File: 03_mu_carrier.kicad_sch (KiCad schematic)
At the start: 42 parts, among them J10 M.2 M-key NVMe (x1), J8 Mu SIO UART debug (verify IO 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, J9 RTC backup coin-cell header, SW2 Mu Power, SW3 Mu Reset, U6 SY8253ADC VSYS -> SYS_5V, U7 SY8253ADC VSYS -> SYS_3V3, U8 TPS7A0210 (VL822 1.0V), U9 VL822-Q7, Y3 25MHz (VL822)

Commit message: Publish the current Ducktop2 design
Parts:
- removed C40: 10u VIN, Capacitor_SMD:C_1206_3216Metric, symbol Device:C
- removed C41: 100n BOOT, Capacitor_SMD:C_0603_1608Metric, symbol Device:C
- removed C52: 1u IN, Capacitor_SMD:C_0805_2012Metric, symbol Device:C
- removed C53: 1u OUT, Capacitor_SMD:C_0805_2012Metric, symbol Device:C
- removed C54, C55, C56, C57, C58, C59: 100n hub bypass, Capacitor_SMD:C_0603_1608Metric, symbol Device:C
- removed C60, C61, C62, C63: 100n hub 1V0 bypass, Capacitor_SMD:C_0603_1608Metric, symbol Device:C
- removed C64, C65: 18p, Capacitor_SMD:C_0603_1608Metric, symbol Device:C
- removed U6: SY8253ADC VSYS -> SYS_5V, Package_TO_SOT_SMD:TSOT-23-6, symbol ducktop2:SY8253ADC
- removed U8: TPS7A0210 (VL822 1.0V), ducktop2:X2SON-4_1.0x1.0mm_P0.65mm, symbol ducktop2:TPS7A0210
- removed U9: VL822-Q7, ducktop2:QFN-76-1EP_9x9mm_P0.4mm_EP6.3x6.3mm, symbol ducktop2:VL822-Q7
- removed Y3: 25MHz (VL822), Crystal:Crystal_SMD_3225-4Pin_3.2x2.5mm, symbol Device:Crystal_GND24
- added C44, C45, C792: 22u 16V X7R TPS56637 OUT, Capacitor_SMD:C_1206_3216Metric, symbol Device:C
- added C586, C587, C66, C67: 100n 10V X7R Mu USB3 TX AC, Capacitor_SMD:C_0402_1005Metric, symbol Device:C
- added C590, C591: 220n 10V X7R Wi-Fi TX AC, Capacitor_SMD:C_0402_1005Metric, symbol Device:C
- added C592, C593, C594, C595, C596, C597, C68, C69: 220n 10V X7R NVMe TX AC, Capacitor_SMD:C_0402_1005Metric, symbol Device:C
- added C750: 68u 50V hybrid input bulk, Capacitor_SMD:CP_Elec_8x10, symbol Device:C_Polarized
- added C751, C752: 10u 50V X7R input, Capacitor_SMD:C_1206_3216Metric, symbol Device:C
- added C753: 1u 50V X5R input, Capacitor_SMD:C_0603_1608Metric, symbol Device:C
- added C754, C755: 100n 50V X7R input HF, Capacitor_SMD:C_0402_1005Metric, symbol Device:C
- added C756, C757: 100n 50V X7R output HF, Capacitor_SMD:C_0402_1005Metric, symbol Device:C
- added C758: 1u 50V X5R output, Capacitor_SMD:C_0603_1608Metric, symbol Device:C
- added C759, C760, C761: 10u 50V X7R output, Capacitor_SMD:C_1206_3216Metric, symbol Device:C
- added C762: 100u 35V hybrid output bulk, Capacitor_SMD:CP_Elec_6.3x5.8, symbol Device:C_Polarized
- added C763: 1u 50V post-sense load-side bypass, Capacitor_SMD:C_0603_1608Metric, symbol Device:C
- added C764: 22u 16V X7R VCC mandatory; effective >4.7u, Capacitor_SMD:C_1206_3216Metric, symbol Device:C
- added C765, C766: 100n 50V X8L bootstrap, Capacitor_SMD:C_0603_1608Metric, symbol Device:C
- added C767: 10n DITH/SYNC spreading, Capacitor_SMD:C_0603_1608Metric, symbol Device:C
- added C768, C769: DNP 2.2n 250V X7R switch-node snubber, Capacitor_SMD:C_0805_2012Metric, symbol Device:C
- added C770: 100n differential current-sense filter, Capacitor_SMD:C_0603_1608Metric, symbol Device:C
- added C771: 4.7n COMP, Capacitor_SMD:C_0603_1608Metric, symbol Device:C
- added C772: 100p C0G COMP HF, Capacitor_SMD:C_0603_1608Metric, symbol Device:C
- added C773: 100n UVLO noise filter, Capacitor_SMD:C_0603_1608Metric, symbol Device:C
- added C774: 10n PG deglitch, Capacitor_SMD:C_0603_1608Metric, symbol Device:C
- added C775: 10n CC deglitch, Capacitor_SMD:C_0603_1608Metric, symbol Device:C
- added C790: 10u 50V X7R TPS56637 VIN, Capacitor_SMD:C_1206_3216Metric, symbol Device:C
- added C791: 100n 50V X7R TPS56637 VIN HF, Capacitor_SMD:C_0603_1608Metric, symbol Device:C
- added C793: 100n qualified host-active gate local, Capacitor_SMD:C_0603_1608Metric, symbol Device:C
- added C794: 1u internal host VBUS switch input, Capacitor_SMD:C_0805_2012Metric, symbol Device:C
- added C830: 10u internal host VBUS output, Capacitor_SMD:C_1206_3216Metric, symbol Device:C
- added C831: 100n internal VBUS supervisor local, Capacitor_SMD:C_0603_1608Metric, symbol Device:C
- added C832: 1u PCIe endpoint switch input, Capacitor_SMD:C_0805_2012Metric, symbol Device:C
- added C833: 4.7n PCIe endpoint controlled slew, Capacitor_SMD:C_0402_1005Metric, symbol Device:C
- added C834: 47u 6.3V PCIe endpoint rail bulk, Capacitor_SMD:C_1206_3216Metric, symbol Device:C
- added C835: 100n PCIe endpoint rail HF, Capacitor_SMD:C_0603_1608Metric, symbol Device:C
- added C836: 10u 6.3V NVMe socket local bulk, Capacitor_SMD:C_1206_3216Metric, symbol Device:C
- added C837: 100n NVMe socket local HF, Capacitor_SMD:C_0603_1608Metric, symbol Device:C
- added H1: Wurth 9774055243R Mu M2 standoff 5.5mm A, ducktop2:Wurth_9774055243R_M2_H5.5, symbol Mechanical:MountingHole_Pad
- added H10, H11, H12, H13, H14, H15, H16, H17: M2.5 isolated mainboard mounting hole, MountingHole:MountingHole_2.7mm_M2.5, symbol Mechanical:MountingHole
- added H2: Wurth 9774055243R Mu M2 standoff 5.5mm B, ducktop2:Wurth_9774055243R_M2_H5.5, symbol Mechanical:MountingHole_Pad
- added H3: M.2 M-key 2280 M2 grounded standoff 2.5mm, ducktop2:SMT_Standoff_M2_H2.5_C4_Tail2.7x1.5, symbol Mechanical:MountingHole_Pad
- added L750: 4.7uH 10.1A Isat / 6.9A Irms, Inductor_SMD:L_Coilcraft_XAL7030-472, symbol Device:L
- added Q750: BSS138 fail-off EN/UVLO clamp, Package_TO_SOT_SMD:SOT-23, symbol Q_NMOS_SOT23_GSD:Q_NMOS_SOT23_GSD
- added Q751: BSS138 active-high enable release, Package_TO_SOT_SMD:SOT-23, symbol Q_NMOS_SOT23_GSD:Q_NMOS_SOT23_GSD
- added R40: 76.8k 0.1% TPS56637 FB high, Resistor_SMD:R_0603_1608Metric, symbol Device:R
- added R41: 10k 0.1% TPS56637 FB low, Resistor_SMD:R_0603_1608Metric, symbol Device:R
- added R42, R770: 169k 1% TPS56637 EN high, Resistor_SMD:R_0603_1608Metric, symbol Device:R
- added R50: 1k NVMe CLKREQ# low: request REFCLK, Resistor_SMD:R_0603_1608Metric, symbol Device:R
- added R750: 10R ISP Kelvin filter, Resistor_SMD:R_0603_1608Metric, symbol Device:R
- added R751: 10R ISN Kelvin filter, Resistor_SMD:R_0603_1608Metric, symbol Device:R
- added R752: 49.9R FB isolation, Resistor_SMD:R_0603_1608Metric, symbol Device:R
- added R753: 102k 0.1% 12V FB high, Resistor_SMD:R_0603_1608Metric, symbol Device:R
- added R754: 11.3k 0.1% 12V FB low, Resistor_SMD:R_0603_1608Metric, symbol Device:R
- added R755: 15k COMP series, Resistor_SMD:R_0603_1608Metric, symbol Device:R
- added R756: 49.9k 1% FSW = 400kHz, Resistor_SMD:R_0603_1608Metric, symbol Device:R
- added R757: 0R MODE forced-PWM, Resistor_SMD:R_0603_1608Metric, symbol Device:R
- added R758: 0R EXTVCC selects internal LDO, Resistor_SMD:R_0603_1608Metric, symbol Device:R
- added R759: 150k 1% UVLO high; 9.0V rising, Resistor_SMD:R_0603_1608Metric, symbol Device:R
- added R760: 23.7k 1% UVLO low, Resistor_SMD:R_0603_1608Metric, symbol Device:R
- added R761: 100k fail-off gate divider low, Resistor_SMD:R_0603_1608Metric, symbol Device:R
- added R762: 100k PG pull-up, Resistor_SMD:R_0603_1608Metric, symbol Device:R
- added R763: 100k CC pull-up, Resistor_SMD:R_0603_1608Metric, symbol Device:R
- added R764, R765: DNP 2.2R 0.25W switch-node snubber, Resistor_SMD:R_1206_3216Metric, symbol Device:R
- added R766: 100k fail-off gate divider high, Resistor_SMD:R_0603_1608Metric, symbol Device:R
- added R767: 100k MU_12V_ENABLE reset pulldown, Resistor_SMD:R_0603_1608Metric, symbol Device:R
- added R768: 10k LattePanda PSON required pull-up, Resistor_SMD:R_0603_1608Metric, symbol Device:R
- added R769: 100k MU_HOST_ACTIVE fail-low, Resistor_SMD:R_0603_1608Metric, symbol Device:R
- added R771: 36.1k 1% TPS56637 EN low, Resistor_SMD:R_0603_1608Metric, symbol Device:R
- added R772: 100k SYS_3V3 PG pull-up, Resistor_SMD:R_0603_1608Metric, symbol Device:R
- added R773: 43.2k 1% internal host VBUS 0.61A ILIM, Resistor_SMD:R_0603_1608Metric, symbol Device:R
- added R774: 10k internal host VBUS fault pull-up, Resistor_SMD:R_0603_1608Metric, symbol Device:R
- added R775: 10k internal host VBUS valid pull-up, Resistor_SMD:R_0603_1608Metric, symbol Device:R
- added R776: 100k PCIe endpoint rail fail-low, Resistor_SMD:R_0603_1608Metric, symbol Device:R
- added RS750: 15mOhm 1% 1W; 3.33A output current limit, Resistor_SMD:R_1206_3216Metric, symbol Device:R
- added SW2: Mu Power, Button_Switch_SMD:SW_SPST_B3S-1000, symbol Switch:SW_Push
- added TP12: MU_12V_PG test, TestPoint:TestPoint_Pad_D1.0mm, symbol Connector:TestPoint
- added TP13: Internal USB VBUS test, TestPoint:TestPoint_Pad_D1.0mm, symbol Connector:TestPoint
- added TP14: Internal USB VBUS valid test, TestPoint:TestPoint_Pad_D1.0mm, symbol Connector:TestPoint
- added TP15: Internal USB VBUS fault test, TestPoint:TestPoint_Pad_D1.0mm, symbol Connector:TestPoint
- added TP5: SYS_5V test, TestPoint:TestPoint_Pad_D1.0mm, symbol Connector:TestPoint
- added TP6: SYS_3V3 test, TestPoint:TestPoint_Pad_D1.0mm, symbol Connector:TestPoint
- added TP8: MU_12V test, TestPoint:TestPoint_Pad_D1.0mm, symbol Connector:TestPoint
- added U6: TPS56637RPAR VSYS -> SYS_5V (5.10V, 6A class), ducktop2:Texas_RPA0010A_VQFN-HR-10_3x3mm, symbol TPS56637:TPS56637
- added U7: TPS56637RPAR VSYS -> SYS_3V3 (3.32V, 6A class), ducktop2:Texas_RPA0010A_VQFN-HR-10_3x3mm, symbol TPS56637:TPS56637
- added U750: TPS552892RYQR 12V buck-boost, ducktop2:Texas_RYQ0021A_VQFN-HR-21_3x5mm, symbol TPS552892:TPS552892
- added U769: SN74LVC1G08DBVR qualified host-active AND, Package_TO_SOT_SMD:SOT-23-5, symbol 74xGxx:74LVC1G08
- added U770: TPS2553DDBVR internal host VBUS 0.61A, Package_TO_SOT_SMD:SOT-23-6, symbol TPS2553D:TPS2553D
- added U771: TLV803EA43RDBZR 4.38V physical internal VBUS supe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, Package_TO_SOT_SMD:SOT-23-3, symbol TLV803EA43RDBZR:TLV803EA43RDBZR
- added U772: TPS22975NDSGR switched PCIe endpoint 3V3, Package_SON:Texas_DSG0008A_WSON-8-1EP_2x2mm_P0.5mm_EP0.9x1.6mm, symbol TPS22975N:TPS22975N
- A1: value LattePanda Mu -> TE 2309411-1 LattePanda Mu host socket/interface; BIOSProfile (none) -> DFLT S70NC1R200-16G-B.bin; SHA256 6edcfe021d84baf2b6ea3e4f4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; MPN (none) -> 2309411-1; Manufacturer (none) -> TE Connectivity; ModuleAssemblyItem (none) -> A2 DFRobot DFR1149; SocketHeight (none) -> 8.0mm standard orientation
- A2: renamed from SW2; value Mu Power -> DFR1149 LattePanda Mu N305 16GB/64GB removable module; footprint Button_Switch_SMD:SW_SPST_B3S-1000 -> (none); symbol Switch:SW_Push -> Mechanical:MountingHole; AssemblyType (none) -> Customer-fitted removable compute module; BIOSProfile (none) -> DFLT S70NC1R200-16G-B.bin; build 2026-06-03; SHA256 6edcfe0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; MPN (none) -> DFR1149; Manufacturer (none) -> DFRobot; RequiredSocket (none) -> A1 TE Connectivity 2309411-1
- C40: renamed from R40; value 732k 1% -> 10u 50V X7R TPS56637 VIN; footprint Resistor_SMD:R_0603_1608Metric -> Capacitor_SMD:C_1206_3216Metric; symbol Device:R -> Device:C; MPN (none) -> CGA5L1X7R1H106K160AC; Manufacturer (none) -> TDK
- C41: renamed from R41; value 100k 1% -> 10u 50V X7R TPS56637 VIN; footprint Resistor_SMD:R_0603_1608Metric -> Capacitor_SMD:C_1206_3216Metric; symbol Device:R -> Device:C; MPN (none) -> CGA5L1X7R1H106K160AC; Manufacturer (none) -> TDK
- C42: value 22u OUT -> 100n 50V X7R TPS56637 VIN HF; footprint Capacitor_SMD:C_1206_3216Metric -> Capacitor_SMD:C_0603_1608Metric
- C43: renamed from U7; value SY8253ADC VSYS -> SYS_3V3 -> 100n 16V X7R TPS56637 BOOT; footprint Package_TO_SOT_SMD:TSOT-23-6 -> Capacitor_SMD:C_0603_1608Metric; symbol ducktop2:SY8253ADC -> Device:C
- C46: value 10u VIN -> 10u 50V X7R TPS56637 VIN; MPN (none) -> CGA5L1X7R1H106K160AC; Manufacturer (none) -> TDK
- C47: value 100n BOOT -> 100n 16V X7R TPS56637 BOOT
- C48: value 22u OUT -> 22u 16V X7R TPS56637 OUT; MPN (none) -> GRM31CZ71C226ME15L; Manufacturer (none) -> Murata
- J10: value M.2 M-key NVMe (x1) -> Amphenol MDT420M01001 M-key NVMe socket (PCIe x4); footprint Connector_PCBEdge:M.2_2280-xx-M -> ducktop2:Amphenol_MDT420M01001_H4.2; MPN (none) -> MDT420M01001; Manufacturer (none) -> Amphenol
- J8: value Mu SIO UART debug (verify IO voltage) -> DNP Mu SIO UART debug (IO voltage unverified); now not fitted; now left out of the parts list
- J9: footprint Connector_PinHeader_2.54mm:PinHeader_1x02_P2.54mm_Vertical -> Connector_JST:JST_GH_SM02B-GHS-TB_1x02-1MP_P1.25mm_Horizontal; Contacts (none) -> SSHL-002T-P0.2; MPN (none) -> SM02B-GHS-TB; Manufacturer (none) -> JST; MatingHousing (none) -> GHR-02V-S
- L4: value 2.2uH >=4.3A -> XAL7070-332MEC 3.3uH 19.4A Isat30%; footprint Inductor_SMD:L_1210_3225Metric -> Inductor_SMD:L_Coilcraft_XAL7070-XXX; MPN (none) -> XAL7070-332MEC; Manufacturer (none) -> Coilcraft
- L5: value 2.2uH >=4.3A -> XAL7070-222MEC 2.2uH 19.6A Isat30%; footprint Inductor_SMD:L_1210_3225Metric -> Inductor_SMD:L_Coilcraft_XAL7070-XXX; MPN (none) -> XAL7070-222MEC; Manufacturer (none) -> Coilcraft
- R43: value 450k 1% -> 45.3k 1% TPS56637 FB high
- R44: value 100k 1% -> 10k 1% TPS56637 FB low
- R45: value 12.1k (verify VL822 REXT) -> 36.1k 1% TPS56637 EN low
- R46: value 100k -> 100k SYS_5V PG pull-up
- SW3: MPN (none) -> B3S-1000; Manufacturer (none) -> Omron
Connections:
- net BUCK33_BOOT: now also U7.7 (BOOT); no longer C43.1 (BOOST)
- net BUCK33_FB: now also U7.2 (FB); no longer C43.3 (FB)
- net BUCK33_SW: now also U7.6 (SW); no longer C43.6 (SW)
- net BUCK5_BOOT: now also C43.1, U6.7 (BOOT)
- net BUCK5_FB: now also R40.2, R41.1, U6.2 (FB); no longer C40.2, C41.1
- net BUCK5_SW: now also C43.2, U6.6 (SW)
- net GND: now also C40.2, C44.2, C45.2, C750.2, C751.2, C752.2, C753.2, C754.2, C755.2, C756.2, C757.2, C758.2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; no longer A2.2, C43.2 (GND)
- net MU_PWRBTN_N: now also SW2.1; no longer A2.1
- net PCIE_M_REFCLK_SRC_N: now also A1.99 (REFCLK2-); no longer A1.87 (REFCLK0-)
- net PCIE_M_REFCLK_SRC_P: now also A1.97 (REFCLK2+); no longer A1.85 (REFCLK0+)
- net SYS_3V3: now also C792.1, C832.1, TP6.1, U772.1 (VIN), U772.2 (VIN), U772.4 (VBIAS); no longer J10.12 (3.3V), J10.14 (3.3V), J10.16 (3.3V), J10.18 (3.3V), J10.2 (3.3V), J10.4 (3.3V), J10.70 (3.3V), J10.72 (3.3V), J10.74 (3.3V), R46.1
- net SYS_5V: now also C44.1, C45.1, C794.1, R40.1, TP5.1, U770.1 (IN); no longer C40.1, C42.1
- net VSYS: now also C40.1, C41.1, C42.1, C750.1, C751.1, C752.1, C753.1, C754.1, C755.1, C790.1, C791.1, R42.1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; no longer A1.250 (VIN), A1.251 (VIN), A1.252 (VIN), A1.253 (VIN), A1.254 (VIN), A1.255 (VIN), A1.256 (VIN), A1.257 (VIN), A1.258 (VIN), A1.259 (VIN), A1.260 (VIN), C43.4 (EN)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
- net WIFI_PCIE_RX_N: now also A1.36 (HSIO3_RX-); no longer A1.24 (HSIO1_RX-)
- net WIFI_PCIE_RX_P: now also A1.34 (HSIO3_RX+); no longer A1.22 (HSIO1_RX+)
- net WIFI_PCIE_TX_N: now also C591.2; no longer A1.21 (HSIO1_TX-)
- net WIFI_PCIE_TX_P: now also C590.2; no longer A1.19 (HSIO1_TX+)
- net WIFI_REFCLK_N: now also A1.90 (REFCLK3-); no longer A1.93 (REFCLK1-)
- net WIFI_REFCLK_P: now also A1.88 (REFCLK3+); no longer A1.91 (REFCLK1+)
- net GBE_CLKREQ_N: now reaches A1.102 (~{CLKREQ4})
- net MU_USB_OC_N: now reaches A1.129 (~{USB_OC})
- net WIFI_PCIE_TX_RAW_P: now reaches A1.31 (HSIO3_TX+)
- net WIFI_PCIE_TX_RAW_P: now also C590.1
- net WIFI_PCIE_TX_RAW_N: now reaches A1.33 (HSIO3_TX-)
- net WIFI_PCIE_TX_RAW_N: now also C591.1
- net PCIE_M_L0_TX_RAW_P: now reaches A1.37 (HSIO8_TX+)
- net PCIE_M_L0_TX_RAW_P: now also C68.1
- net PCIE_M_L0_TX_RAW_N: now reaches A1.39 (HSIO8_TX-)
- net PCIE_M_L0_TX_RAW_N: now also C69.1
- net PCIE_M_L0_RX_P: now reaches A1.40 (HSIO8_RX+)
- net PCIE_M_L0_RX_P: now also J10.43 (PERp0/SATA-B-)
- net PCIE_M_L0_RX_N: now reaches A1.42 (HSIO8_RX-)
- net PCIE_M_L0_RX_N: now also J10.41 (PERn0/SATA-B+)
- net PCIE_M_L1_TX_RAW_P: now reaches A1.43 (HSIO9_TX+)
- net PCIE_M_L1_TX_RAW_P: now also C592.1
- net PCIE_M_L1_TX_RAW_N: now reaches A1.45 (HSIO9_TX-)
- net PCIE_M_L1_TX_RAW_N: now also C593.1
- net PCIE_M_L1_RX_P: now reaches A1.46 (HSIO9_RX+)
- net PCIE_M_L1_RX_P: now also J10.31 (PERp1)
- net PCIE_M_L1_RX_N: now reaches A1.48 (HSIO9_RX-)
- net PCIE_M_L1_RX_N: now also J10.29 (PERn1)
- net PCIE_M_L2_TX_RAW_P: now reaches A1.49 (HSIO10_TX+)
- net PCIE_M_L2_TX_RAW_P: now also C594.1
- net MU_S0_HIGH: now reaches A1.5 (PSON)
- net MU_S0_HIGH: now also R768.2, U769.1
- net PCIE_M_L2_TX_RAW_N: now reaches A1.51 (HSIO10_TX-)
- net PCIE_M_L2_TX_RAW_N: now also C595.1
- net PCIE_M_L2_RX_P: now reaches A1.52 (HSIO10_RX+)
- net PCIE_M_L2_RX_P: now also J10.19 (PERp2)
- net PCIE_M_L2_RX_N: now reaches A1.54 (HSIO10_RX-)
- net PCIE_M_L2_RX_N: now also J10.17 (PERn2)
- net PCIE_M_L3_TX_RAW_P: now reaches A1.55 (HSIO11_TX+)
- net PCIE_M_L3_TX_RAW_P: now also C596.1
- net PCIE_M_L3_TX_RAW_N: now reaches A1.57 (HSIO11_TX-)
- net PCIE_M_L3_TX_RAW_N: now also C597.1
- net PCIE_M_L3_RX_P: now reaches A1.58 (HSIO11_RX+)
- net PCIE_M_L3_RX_P: now also J10.7 (PERp3)
- net PCIE_M_L3_RX_N: now reaches A1.60 (HSIO11_RX-)
- net PCIE_M_L3_RX_N: now also J10.5 (PERn3)
- net GBE_HOST_TX_P: now reaches A1.61 (HSIO6_TX+)
- net GBE_HOST_TX_N: now reaches A1.63 (HSIO6_TX-)
- net GBE_HOST_RX_P: now reaches A1.64 (HSIO6_RX+)
- net GBE_HOST_RX_N: now reaches A1.66 (HSIO6_RX-)
- net GBE_REFCLK_P: now reaches A1.94 (REFCLK4+)
- net GBE_REFCLK_N: now reaches A1.96 (REFCLK4-)
- net PCIE_M_L3_TX_N: now reaches J10.11 (PETn3)
- net PCIE_M_L3_TX_N: now also C597.2
- net PCIE_M_L3_TX_P: now reaches J10.13 (PETp3)
- net PCIE_M_L3_TX_P: now also C596.2
- net PCIE_M_L2_TX_N: now reaches J10.23 (PETn2)
- net PCIE_M_L2_TX_N: now also C595.2
- net PCIE_M_L2_TX_P: now reaches J10.25 (PETp2)
- net PCIE_M_L2_TX_P: now also C594.2
- net PCIE_M_L1_TX_N: now reaches J10.35 (PETn1)
- net PCIE_M_L1_TX_N: now also C593.2
- net PCIE_M_L1_TX_P: now reaches J10.37 (PETp1)
- net PCIE_M_L1_TX_P: now also C592.2
- net PCIE_M_CLKREQ_N: now reaches J10.52 (~{CLKREQ})
- net PCIE_M_CLKREQ_N: now also R50.1
- net DDIB_DDC_SCL: no longer names the net of A1.171 (DDIB_DDC_SCL)
- net DDIB_DDC_SDA: no longer names the net of A1.169 (DDIB_DDC_SDA)
- net DDIB_HPD: no longer names the net of A1.183 (DDIB_HPD)
- net DDIB_TX0_N: no longer names the net of A1.215 (DDIB_TX0-)
- net DDIB_TX0_P: no longer names the net of A1.217 (DDIB_TX0+)
- net DDIB_TX1_N: no longer names the net of A1.209 (DDIB_TX1-)
- net DDIB_TX1_P: no longer names the net of A1.211 (DDIB_TX1+)
- net DDIB_TX2_N: no longer names the net of A1.203 (DDIB_TX2-)
- net DDIB_TX2_P: no longer names the net of A1.205 (DDIB_TX2+)
- net DDIB_TX3_N: no longer names the net of A1.197 (DDIB_TX3-)
- net DDIB_TX3_P: no longer names the net of A1.199 (DDIB_TX3+)
- net HUB_REXT renamed BUCK5_EN
- net BUCK5_EN: now also R42.2, U6.1 (EN)
- net HUB_UP_DM renamed USBC1_DM
- net HUB_UP_DP renamed USBC1_DP
- net HUB_UP_RX_N renamed USBC1_SSRX_N
- net HUB_UP_RX_P renamed USBC1_SSRX_P
- net HUB_UP_TX_N renamed USBC1_SSTX_RAW_N
- net USBC1_SSTX_RAW_N: now also C67.1
- net HUB_UP_TX_P renamed USBC1_SSTX_RAW_P
- net USBC1_SSTX_RAW_P: now also C66.1
- net HUB_UP_VBUS_DET renamed SYS_5V_PG
- net SYS_5V_PG: now also U6.4 (PG)
- net PCIE_M_RX_N: no longer names the net of A1.30 (HSIO2_RX-)
- net PCIE_M_RX_N: no longer J10.47 (PETn0/SATA-A-)
- net PCIE_M_RX_P: no longer names the net of A1.28 (HSIO2_RX+)
- net PCIE_M_RX_P: no longer J10.49 (PETp0/SATA-A+)
- net PCIE_M_TX_N: no longer names the net of A1.27 (HSIO2_TX-)
- net PCIE_M_TX_N: no longer J10.41 (PERn0/SATA-B+)
- net PCIE_M_TX_P: no longer names the net of A1.25 (HSIO2_TX+)
- net PCIE_M_TX_P: no longer J10.43 (PERp0/SATA-B-)
- net TOUCH_USB_DM renamed USBC2_DM
- net TOUCH_USB_DP renamed USBC2_DP
- new net BUCK33_EN: R770.2, R771.1, U7.1 (EN)
- new net INTERNAL_USB_VBUS: C830.1, C831.1, TP13.1, U770.6 (OUT), U771.3 (VDD)
- new net INTERNAL_USB_VBUS_FAULT_N: R774.2, TP15.1, U770.4 (~{FAULT})
- new net INTERNAL_USB_VBUS_ILIM: R773.1, U770.5 (ILIM)
- new net INTERNAL_USB_VBUS_VALID: R775.2, TP14.1, U771.1 (RESETz)
- new net MCU_3V3: C793.1, R46.1, R762.1, R768.1, R772.1, R774.1, R775.1, U769.5 (VCC)
- new net MU12_BOOT1: C765.1, U750.20 (BOOT1)
- new net MU12_BOOT2: C766.1, U750.19 (BOOT2)
- new net MU12_CC_N: C775.1, R763.2, U750.4 (~{CC})
- new net MU12_COMP: C772.1, R755.1, U750.15 (COMP)
- new net MU12_COMP_RC: C771.1, R755.2
- new net MU12_DITH: C767.1, U750.5 (DITH/SYNC)
- new net MU12_EN_UVLO: C773.1, Q750.3 (D), R759.2, R760.1, U750.1 (EN/UVLO)
- new net MU12_EXTVCC: R758.2, U750.21 (EXTVCC)
- new net MU12_FB: R753.2, R754.1, U750.14 (FB)
- new net MU12_FB_TOP: R752.2, R753.1
- new net MU12_FORCE_OFF: Q750.1 (G), Q751.3 (D), R761.1, R766.2
- new net MU12_FSW: R756.1, U750.6 (FSW)
- new net MU12_ISN: C770.2, R751.2, U750.13 (ISN)
- new net MU12_ISP: C770.1, R750.2, U750.12 (ISP)
- new net MU12_MODE: R757.2, U750.2 (MODE)
- new net MU12_PRE_SENSE: C756.1, C757.1, C758.1, C759.1, C760.1, C761.1, C762.1, R750.1, RS750.1, U750.11 (VOUT)
- new net MU12_SNUB1: C768.1, R764.2
- new net MU12_SNUB2: C769.1, R765.2
- new net MU12_SW1: C765.2, L750.1, R764.1, U750.8 (SW1)
- new net MU12_SW2: C766.2, L750.2, R765.1, U750.10 (SW2)
- new net MU12_VCC: C764.1, R757.1, R758.1, R763.1, U750.18 (VCC)
- new net MU_12V: A1.250 (VIN), A1.251 (VIN), A1.252 (VIN), A1.253 (VIN), A1.254 (VIN), A1.255 (VIN), A1.256 (VIN), A1.257 (VIN), A1.258 (VIN), A1.259 (VIN), A1.260 (VIN), C763.1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
- new net MU_12V_ENABLE: Q751.1 (G), R767.1
- new net MU_12V_PG: C774.1, R762.2, TP12.1, U750.3 (PG), U769.2
- new net MU_HOST_ACTIVE: R769.1, R776.1, U769.4, U770.3 (EN), U772.3 (ON)
- new net PCIE_3V3: C834.1, C835.1, C836.1, C837.1, J10.12 (3.3V), J10.14 (3.3V), J10.16 (3.3V), J10.18 (3.3V), J10.2 (3.3V), J10.4 (3.3V), J10.70 (3.3V), J10.72 (3.3V)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
- new net PCIE_3V3_CT: C833.1, U772.6 (CT)
- new net PCIE_M_L0_TX_N: C69.2, J10.47 (PETn0/SATA-A-)
- new net PCIE_M_L0_TX_P: C68.2, J10.49 (PETp0/SATA-A+)
- new net SYS_3V3_PG: R772.2, U7.4 (PG)
- new net USBC1_SSTX_N: C67.2
- new net USBC1_SSTX_P: C66.2
- new net USBC2_SSRX_N: A1.24 (HSIO1_RX-)
- new net USBC2_SSRX_P: A1.22 (HSIO1_RX+)
- new net USBC2_SSTX_N: C587.2
- new net USBC2_SSTX_P: C586.2
- new net USBC2_SSTX_RAW_N: A1.21 (HSIO1_TX-), C587.1
- new net USBC2_SSTX_RAW_P: A1.19 (HSIO1_TX+), C586.1
- no-connect marks 191 -> 136
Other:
- note added: "== J10 M.2 M-key NVMe, default-BIOS PCIe Gen3 x4 =="
- note added: "== U750 TPS552892 VSYS -> regulated MU_12V, 12 V / 3.3 A limit =="
- note added: "Default-BIOS HSIO0/1 are independent native USB 3.2 Gen2 ports; HSIO3 + USB2_P1 feed M.2 E-key."
- note added: "M.2 M-key uses default HSIO8-11 x4 and REFCLK2; no lane reversal and no TX/RX direction swap."
- note added: "M.2 M-key: Mu TX->PET through 220n near J10; PET/PER naming is from the host perspective."
- note added: "MECHANICAL: H3 is the grounded 2280 retainer for the 4.2mm M-key socket. H10-H17 are isolated M2.5 chassis holes; chassis bonding is a separate controlled point."
- note added: "MECHANICAL: the 8.0mm standard-orientation TE 2309411-1 socket requires two grounded 5.5mm M2 standoffs at H1/H2; SO-DIMM clips alone are not structural retention."
- note added: "MU_12V is a TPS552892EVM-derived 12V stage: 400kHz forced PWM, 3.33A nominal limit, and about 8.65-9.40V worst-case rising UVLO. Firmware requires VSYS >=10.0V."
- note added: "MU_12V_ENABLE is active high and defaults low. Q750/Q751 force EN/UVLO low until EC firmware explicitly releases the rail; MU_12V_PG is pulled up to MCU_3V3."
- note added: "MU_S0_HIGH is Mu PSON with the required 10k pull-up to always-on MCU_3V3. It is a weak status signal for logic/NMOS gates only, never a load supply."
- note added: "Mu VIN and onboard eDP BL_PWR use regulated MU_12V; the exact B160QAN03.K harness/pinout remains a release gate."
- note added: "Native USB-C data/OC nets leave to sheet 4; VBUS switching, CC, muxing, and ESD live there."
- note added: "POWER BUDGET HOLD: MU_12V is about 40W maximum for Mu plus eDP backlight. Lock BIOS PL1/PL2 only after measuring panel and whole-module draw; unrestricted 35W CPU mode is not released."
- note added: "SLEEP POLICY: PSON is low in S3, so PCIe endpoint 3V3, user USB-C VBUS, trackpad, maker USB, and internal audio detach. Wake from those devices is intentionally unsupported."
- note added: "SYS_5V and SYS_3V3 use TPS56637 6A-class bucks with XAL7070 inductors; endpoint load budgets remain a release check."
- note added: "The verified B160QAN03.K panel connects to the Mu onboard eDP connector; DDIB is unused."
- note added: "USB2_P3 is EC; P4 pairs with USB-C 2; P5 is the system-audio hub; P7 is maker MCU; P8 is trackpad."
- note removed: "== J10 M.2 M-key NVMe, PCIe x1 only =="
- note removed: "== U9 VL822-Q7 USB3 hub, upstream on Mu HSIO0/USB2_P2 =="
- note removed: "DDIB HDMI 2.0 nets leave to sheet 11 for the retained Intehill monitor/controller path."
- note removed: "HSIO0 + USB2_P2 feed VL822 upstream; HSIO1 + USB2_P1 feed the M.2 E-key radio slot."
- note removed: "M.2 M-key is wired as PCIe x1. CLKREQM is intentionally left NC per DFRobot reference mining."
- note removed: "Mu VIN is tied directly to VSYS; no intermediate module VIN buck."
- note removed: "SYS_5V/SYS_3V3 use 0.6V FB dividers: 732k/100k and 450k/100k; verify compensation before fab."
- note removed: "TPS7A0210 is a real 1.0V part, but sits at the low edge of the VL822 1.0-1.1V rail range."
- note removed: "USB2_P3 is EC; USB2_P4 is touch; USB2_P5 is radio audio; USB2_P7 is maker MCU USB; USB2_P8 is trackpad."
- note removed: "VL822 downstream PE/OC/data leave this sheet; USB-C VBUS/CC/muxing lives on sheet 4."
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
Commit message: Finish USB-C policy and split out radio board
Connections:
- net MU_USB_OC_N renamed PD_PROTECT_FAULT_N
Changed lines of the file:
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@@
 (no_connect (at 200.66 132.08))
 (no_connect (at 200.66 154.94))
-(hierarchical_label "MU_USB_OC_N"
+(hierarchical_label "PD_PROTECT_FAULT_N"
   (shape bidirectional)
   (at 200.66 134.62 0)

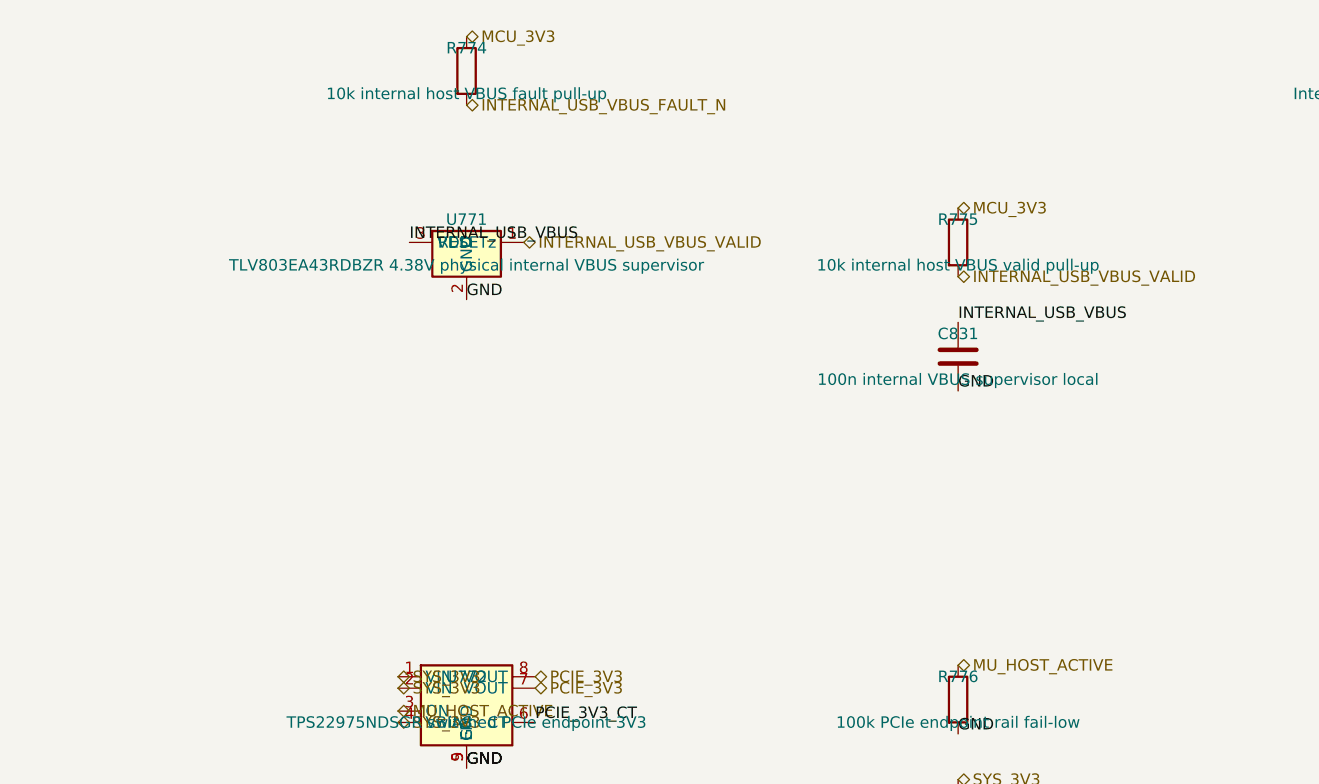
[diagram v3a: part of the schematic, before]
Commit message: Refresh repository with updated PCB renders and current design state
- New 3D renders: top, bottom, perspective, and keyboard PCB
  (generated via kicad-cli 10.0.4, 2560x1440, high quality)
- Update README status: placement complete, coupling caps relocated,
  independent design review CONDITIONAL PASS (2026-07-21)
- Add keyboard rev-A fullboard stencil generation (3MF, STL, manifest, script)
- Track TPS3897ADRYR library symbol
- WIP schematic, PCB, and generator refinements post-coupling-cap fix
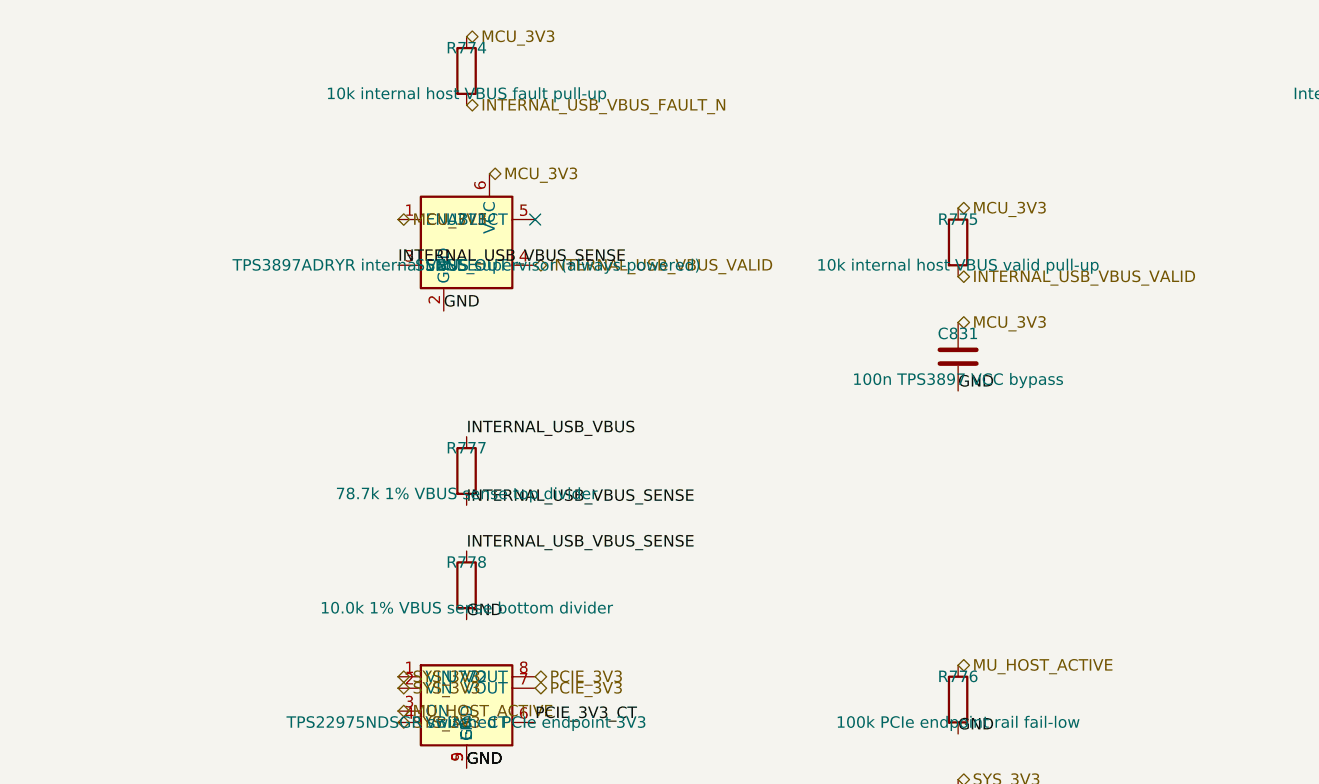
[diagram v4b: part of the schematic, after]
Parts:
- removed C590, C591: 220n 10V X7R Wi-Fi TX AC, Capacitor_SMD:C_0402_1005Metric, symbol Device:C
- removed C597: 220n 10V X7R NVMe TX AC, Capacitor_SMD:C_0402_1005Metric, symbol Device:C
- removed C836: 10u 6.3V NVMe socket local bulk, Capacitor_SMD:C_1206_3216Metric, symbol Device:C
- removed R763: 100k CC pull-up, Resistor_SMD:R_0603_1608Metric, symbol Device:R
- removed TP6: SYS_3V3 test, TestPoint:TestPoint_Pad_D1.0mm, symbol Connector:TestPoint
- added C592: 220n 10V X7R NVMe TX AC, Capacitor_SMD:C_0402_1005Metric, symbol Device:C
- added H13: M2.5 isolated mainboard mounting hole, MountingHole:MountingHole_2.7mm_M2.5, symbol Mechanical:MountingHole
- added R47: 0R / PERST isolation, Resistor_SMD:R_0603_1608Metric, symbol Device:R
- added R48: 0R / REFCLK+ isolation, Resistor_SMD:R_0603_1608Metric, symbol Device:R
- added R49: 0R / REFCLK- isolation, Resistor_SMD:R_0603_1608Metric, symbol Device:R
- added R778: 10.0k 1% VBUS sense bottom divider, Resistor_SMD:R_0603_1608Metric, symbol Device:R
- added TP15: Internal USB VBUS fault test, TestPoint:TestPoint_Pad_D1.0mm, symbol Connector:TestPoint
- added TP5: SYS_5V test, TestPoint:TestPoint_Pad_D1.0mm, symbol Connector:TestPoint
- C590: renamed from R48; value 0R / REFCLK+ isolation -> 220n 10V X7R Wi-Fi TX AC; footprint Resistor_SMD:R_0603_1608Metric -> Capacitor_SMD:C_0402_1005Metric; symbol Device:R -> Device:C; MPN (none) -> GRM155R71A224KE01D; Manufacturer (none) -> Murata
- C591: renamed from R49; value 0R / REFCLK- isolation -> 220n 10V X7R Wi-Fi TX AC; footprint Resistor_SMD:R_0603_1608Metric -> Capacitor_SMD:C_0402_1005Metric; symbol Device:R -> Device:C; MPN (none) -> GRM155R71A224KE01D; Manufacturer (none) -> Murata
- C597: renamed from R47; value 0R / PERST isolation -> 220n 10V X7R NVMe TX AC; footprint Resistor_SMD:R_0603_1608Metric -> Capacitor_SMD:C_0402_1005Metric; symbol Device:R -> Device:C; MPN (none) -> GRM155R71A224KE01D; Manufacturer (none) -> Murata
- C831: value 100n internal VBUS supervisor local -> 100n TPS3897 VCC bypass
- C836: renamed from H13; value M2.5 isolated mainboard mounting hole -> 10u 6.3V NVMe socket local bulk; footprint MountingHole:MountingHole_2.7mm_M2.5 -> Capacitor_SMD:C_1206_3216Metric; symbol Mechanical:MountingHole -> Device:C; Hardware_Spec 2.7mm isolated NPTH for M2.5 chassis screw; no electrical c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 -> (none); MPN (none) -> GRM21BR60J106ME19L; Manufacturer (none) -> Murata; now in the parts list
- R763: renamed from TP5; value SYS_5V test -> 100k CC pull-up; footprint TestPoint:TestPoint_Pad_D1.0mm -> Resistor_SMD:R_0603_1608Metric; symbol Connector:TestPoint -> Device:R; ProcurementClass PCB copper test feature -> (none); now in the parts list
- R777: renamed from TP15; value Internal USB VBUS fault test -> 78.7k 1% VBUS sense top divider; footprint TestPoint:TestPoint_Pad_D1.0mm -> Resistor_SMD:R_0603_1608Metric; symbol Connector:TestPoint -> Device:R; MPN (none) -> RC0603FR-0778K7L; Manufacturer (none) -> Yageo; ProcurementClass PCB copper test feature -> (none); now in the parts list
- TP6: renamed from C592; value 220n 10V X7R NVMe TX AC -> SYS_3V3 test; footprint Capacitor_SMD:C_0402_1005Metric -> TestPoint:TestPoint_Pad_D1.0mm; symbol Device:C -> Connector:TestPoint; MPN GRM155R71A224KE01D -> (none); Manufacturer Murata -> (none); ProcurementClass (none) -> PCB copper test feature; now left out of the parts list
- U771: value TLV803EA43RDBZR 4.38V physical internal VBUS supervisor -> TPS3897ADRYR internal VBUS supervisor (always-powered); footprint Package_TO_SOT_SMD:SOT-23-3 -> Package_SON:Texas_USON-6_1x1.45mm_P0.5mm_SMD; symbol TLV803EA43RDBZR:TLV803EA43RDBZR -> TPS3897ADRYR:TPS3897ADRYR; Function Assert valid only after carrier-generated host VBUS exceeds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 -> Assert VBUS valid only after SENSE (divided INTERNAL_USB_VB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; MPN TLV803EA43RDBZR -> TPS3897ADRYR
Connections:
- net GND: now also C836.2, R778.2
- net INTERNAL_USB_VBUS: now also R777.1; no longer C831.1, U771.3 (VDD)
- net INTERNAL_USB_VBUS_FAULT_N: now also TP15.1; no longer R777.1
- net INTERNAL_USB_VBUS_VALID: now also U771.4 (SENSE_OUT); no longer U771.1 (RESETz)
- net MCU_3V3: now also C831.1, U771.1 (ENABLE), U771.6 (VCC)
- net MU12_CC_N: now also R763.2
- net MU12_VCC: now also R763.1
- net PCIE_3V3: now also C836.1
- net PCIE_M_L1_TX_P: now also C592.2; no longer TP6.2
- net PCIE_M_L1_TX_RAW_P: now also C592.1; no longer TP6.1
- net PCIE_M_L3_TX_N: now also C597.2
- net PCIE_M_L3_TX_RAW_N: now also C597.1
- net PCIE_M_PERST_N: now also R47.2; no longer C597.2
- net PCIE_M_REFCLK_N: now also R49.2; no longer C591.2
- net PCIE_M_REFCLK_P: now also R48.2; no longer C590.2
- net PCIE_M_REFCLK_SRC_N: now also R49.1; no longer C591.1
- net PCIE_M_REFCLK_SRC_P: now also R48.1; no longer C590.1
- net PLTRST_SRC_N: now also R47.1; no longer C597.1
- net SYS_3V3: now also TP6.1
- net SYS_5V: now also TP5.1; no longer R763.1
- net WIFI_PCIE_TX_N: now also C591.2
- net WIFI_PCIE_TX_P: now also C590.2
- net WIFI_PCIE_TX_RAW_N: now also C591.1
- net WIFI_PCIE_TX_RAW_P: now also C590.1
- new net INTERNAL_USB_VBUS_SENSE: R777.2, R778.1, U771.3 (SENSE)
- no-connect marks 136 -> 137
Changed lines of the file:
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@@
 )
 (symbol
-  (lib_id "TLV803EA43RDBZR:TLV803EA43RDBZR")
+  (lib_id "TPS3897ADRYR:TPS3897ADRYR")
   (at 900.43 369.57 0)
   (unit 1)
@@
   (dnp no)
   (property "Reference" "U771" (at 900.43 367.03 0) (effects (font (size 1.27 1.27))))
-  (property "Value" "TLV803EA43RDBZR 4.38V physical internal VBUS supervisor" (at 900.43 372.11 0) (effects (font (size 1.27 1.27))))
-  (property "Footprint" "Package_TO_SOT_SMD:SOT-23-3" (at 900.43 369.57 0) (effects (font (size 1.27 1.27)) (hide yes)))
+  (property "Value" "TPS3897ADRYR internal VBUS supervisor (always-powered)" (at 900.43 372.11 0) (effects (font (size 1.27 1.27))))
+  (property "Footprint" "Package_SON:Texas_USON-6_1x1.45mm_P0.5mm_SMD" (at 900.43 369.57 0) (effects (font (size 1.27 1.27)) (hide yes)))
   (property "Datasheet" "" (at 900.43 369.57 0) (effects (font (size 1.27 1.27)) (hide yes)))
   (property "Manufacturer" "Texas Instruments" (at 900.43 369.57 0) (effects (font (size 1.27 1.27)) (hide yes)))
-  (property "MPN" "TLV803EA43RDBZR" (at 900.43 369.57 0) (effects (font (size 1.27 1.27)) (hide yes)))
-  (property "Datasheet" "https://www.ti.com/lit/ds/symlink/tlv803e.pdf" (at 900.43 369.57 0) (effects (font (size 1.27 1.27)) (hide yes)))
-  (property "Function" "Assert valid only after carrier-generated host VBUS exceeds the 4.38V falling threshold" (at 900.43 369.57 0) (effects (font (size 1.27 1.27)) (hide yes)))
+  (property "MPN" "TPS3897ADRYR" (at 900.43 369.57 0) (effects (font (size 1.27 1.27)) (hide yes)))
+  (property "Datasheet" "https://www.ti.com/lit/ds/symlink/tps3897.pdf" (at 900.43 369.57 0) (effects (font (size 1.27 1.27)) (hide yes)))
+  (property "Function" "Assert VBUS valid only after SENSE (divided INTERNAL_USB_VBUS) exceeds 0.5V threshold; VCC always on MCU_3V3 for deterministic output" (at 900.43 369.57 0) (effects (font (size 1.27 1.27)) (hide yes)))
   (pin "1")
   (pin "2")
   (pin "3")
+  (pin "4")
+  (pin "5")
+  (pin "6")
   (instances
     (project "ducktop2"
@@
   )
 )
-(hierarchical_label "INTERNAL_USB_VBUS_VALID"
+(hierarchical_label "MCU_3V3"
   (shape bidirectional)
-  (at 906.78 369.57 0)
+  (at 892.81 367.03 0)
   (effects (font (size 1.27 1.27)) (justify left bottom))
 )
 (label "GND"
-  (at 900.43 375.92 0)
+  (at 897.89 377.19 0)
   (effects (font (size 1.27 1.27)) (justify left bottom))
 )
-(label "INTERNAL_USB_VBUS"
-  (at 894.08 369.57 0)
+(label "INTERNAL_USB_VBUS_SENSE"
+  (at 892.81 372.11 0)
+  (effects (font (size 1.27 1.27)) (justify left bottom))
+)
+(hierarchical_label "INTERNAL_USB_VBUS_VALID"
+  (shape bidirectional)
+  (at 908.05 372.11 0)
+  (effects (font (size 1.27 1.27)) (justify left bottom))
+)
+(no_connect (at 908.05 367.03))
+(hierarchical_label "MCU_3V3"
+  (shape bidirectional)
+  (at 902.97 361.95 0)
   (effects (font (size 1.27 1.27)) (justify left bottom))
 )
@@
   (dnp no)
   (property "Reference" "C831" (at 955.04 379.73 0) (effects (font (size 1.27 1.27))))
-  (property "Value" "100n internal VBUS supervisor local" (at 955.04 384.81 0) (effects (font (size 1.27 1.27))))
+  (property "Value" "100n TPS3897 VCC bypass" (at 955.04 384.81 0) (effects (font (size 1.27 1.27))))
   (property "Footprint" "Capacitor_SMD:C_0603_1608Metric" (at 955.04 382.27 0) (effects (font (size 1.27 1.27)) (hide yes)))
   (property "Datasheet" "" (at 955.04 382.27 0) (effects (font (size 1.27 1.27)) (hide yes)))
@@
   )
 )
-(label "INTERNAL_USB_VBUS"
+(hierarchical_label "MCU_3V3"
+  (shape bidirectional)
   (at 955.04 378.46 0)
   (effects (font (size 1.27 1.27)) (justify left bottom))
@@
   (effects (font (size 1.27 1.27)) (justify left bottom))
 )
+(symbol
+  (lib_id "Device:R")
+  (at 900.43 394.97 0)
+  (unit 1)
+  (exclude_from_sim no)
+  (in_bom yes)
+  (on_board yes)
+  (dnp no)
+  (property "Reference" "R777" (at 900.43 392.43 0) (effects (font (size 1.27 1.27))))
+  (property "Value" "78.7k 1% VBUS sense top divider" (at 900.43 397.51 0) (effects (font (size 1.27 1.27))))
+  (property "Footprint" "Resistor_SMD:R_0603_1608Metric" (at 900.43 394.97 0) (effects (font (size 1.27 1.27)) (hide yes)))
+  (property "Datasheet" "" (at 900.43 394.97 0) (effects (font (size 1.27 1.27)) (hide yes)))
+  (property "Manufacturer" "Yageo" (at 900.43 394.97 0) (effects (font (size 1.27 1.27)) (hide yes)))
+  (property "MPN" "RC0603FR-0778K7L" (at 900.43 394.97 0) (effects (font (size 1.27 1.27)) (hide yes)))
+  (pin "1")
+  (pin "2")
+  (instances
+    (project "ducktop2"
+      (path "/7f3572a2-a529-5ef0-93eb-27f85c0119a9"
+        (reference "R777")
+        (unit 1)
+      )
+    )
+  )
+)
+(label "INTERNAL_USB_VBUS"
+  (at 900.43 391.16 0)
+  (effects (font (size 1.27 1.27)) (justify left bottom))
+)
+(label "INTERNAL_USB_VBUS_SENSE"
+  (at 900.43 398.78 0)
+  (effects (font (size 1.27 1.27)) (justify left bottom))
+)
+(symbol
+  (lib_id "Device:R")
+  (at 900.43 407.67 0)
+  (unit 1)
+  (exclude_from_sim no)
+  (in_bom yes)
+  (on_board yes)
+  (dnp no)
+  (property "Reference" "R778" (at 900.43 405.13 0) (effects (font (size 1.27 1.27))))
+  (property "Value" "10.0k 1% VBUS sense bottom divider" (at 900.43 410.21 0) (effects (font (size 1.27 1.27))))
+  (property "Footprint" "Resistor_SMD:R_0603_1608Metric" (at 900.43 407.67 0) (effects (font (size 1.27 1.27)) (hide yes)))
+  (property "Datasheet" "" (at 900.43 407.67 0) (effects (font (size 1.27 1.27)) (hide yes)))
+  (property "Manufacturer" "Yageo" (at 900.43 407.67 0) (effects (font (size 1.27 1.27)) (hide yes)))
+  (property "MPN" "RC0603FR-0710KL" (at 900.43 407.67 0) (effects (font (size 1.27 1.27)) (hide yes)))
+  (pin "1")
+  (pin "2")
+  (instances
+    (project "ducktop2"
+      (path "/7f3572a2-a529-5ef0-93eb-27f85c0119a9"
+        (reference "R778")
+        (unit 1)
+      )
+    )
+  )
+)
+(label "INTERNAL_USB_VBUS_SENSE"
+  (at 900.43 403.86 0)
+  (effects (font (size 1.27 1.27)) (justify left bottom))
+)
+(label "GND"
+  (at 900.43 411.48 0)
+  (effects (font (size 1.27 1.27)) (justify left bottom))
+)
